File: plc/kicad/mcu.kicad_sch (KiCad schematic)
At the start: 58 parts, among them J1 Conn_01x03_Pin, J2 Conn_01x04_Pin, Q3 L8050QLT1G, Q4 L8050QLT1G, SW1 TSD003B08026A03, SW2 TSD003B08026A03, U10 ESP32-S3-MINI-1U, U11 BS-0601-SK-4W, U12 AHT20_C2757850, U13 CP2102N-A02-GQFN28R, U9 RV-3028-C7

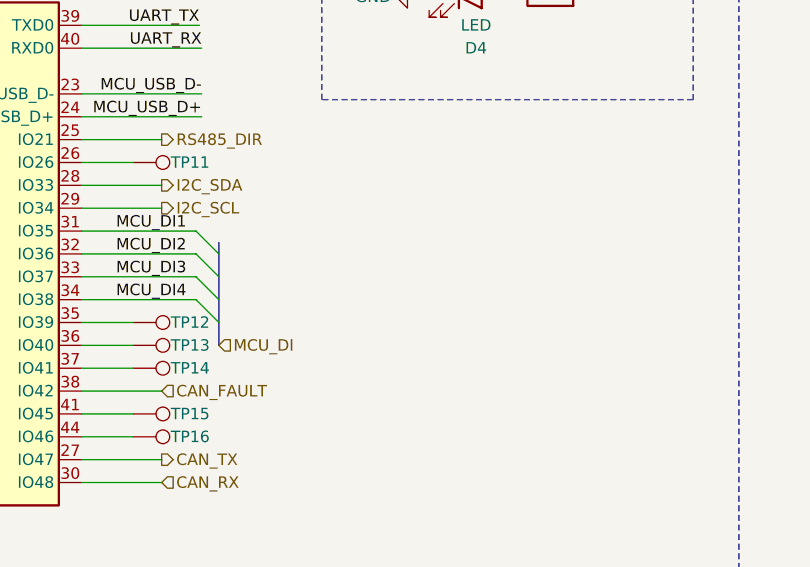
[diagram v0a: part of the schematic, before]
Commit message: Updated PCB placement
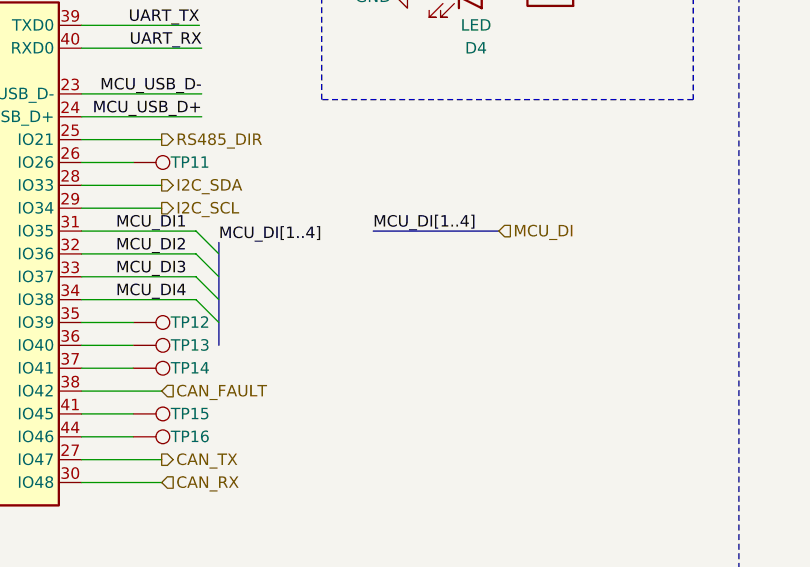
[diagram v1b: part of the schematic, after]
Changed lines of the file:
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@@
+		)
+	)
+	(bus
+		(pts
+			(xy 158.115 72.39) (xy 172.085 72.39)
+		)
+		(stroke
+			(width 0)
+			(type default)
 		)
 	)
@@
 		)
 	)
+	(label "MCU_DI[1..4]"
+		(at 158.115 72.39 0)
+		(effects
+			(font
+				(size 1.27 1.27)
+			)
+			(justify left bottom)
+		)
+	)
 	(label "SD_CD"
 		(at 84.455 77.47 0)
@@
 			)
 			(justify right bottom)
+		)
+	)
+	(label "MCU_DI[1..4]"
+		(at 140.97 73.66 0)
+		(effects
+			(font
+				(size 1.27 1.27)
+			)
+			(justify left bottom)
 		)
 	)
@@
 		)
 	)
+	(hierarchical_label "MCU_DI"
+		(shape input)
+		(at 172.085 72.39 0)
+		(effects
+			(font
+				(size 1.27 1.27)
+			)
+			(justify left)
+		)
+	)
 	(hierarchical_label "I2C_SCL"
 		(shape input)
@@
 		)
 	)
-	(hierarchical_label "MCU_DI"
-		(shape input)
-		(at 140.97 85.09 0)
-		(effects
-			(font
-				(size 1.27 1.27)
-			)
-			(justify left)
-		)
-	)

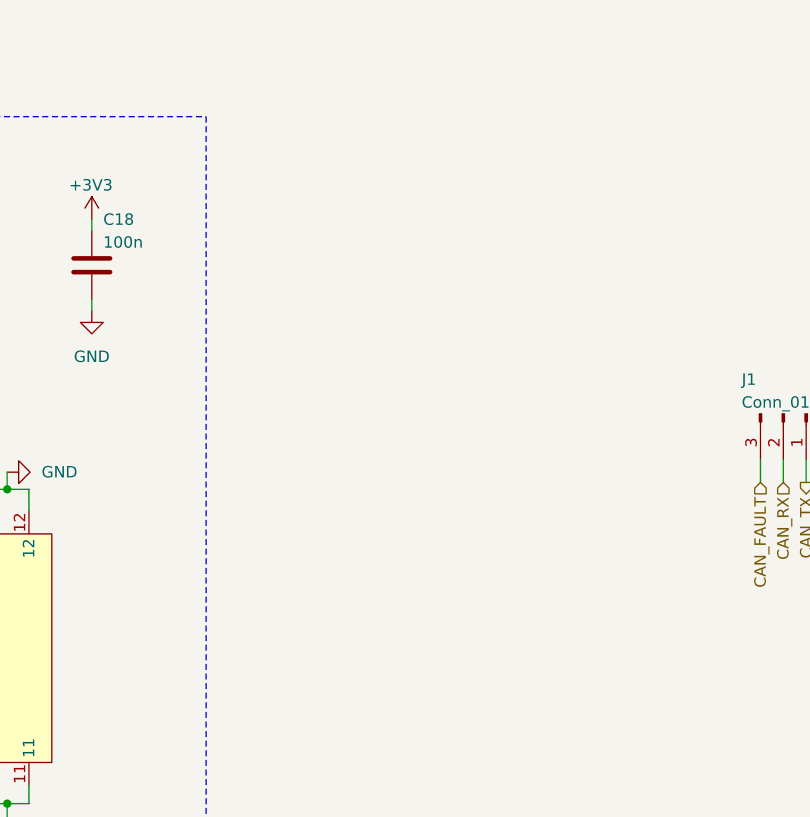
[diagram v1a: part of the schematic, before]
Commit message: Added mounting holes & PCB outline
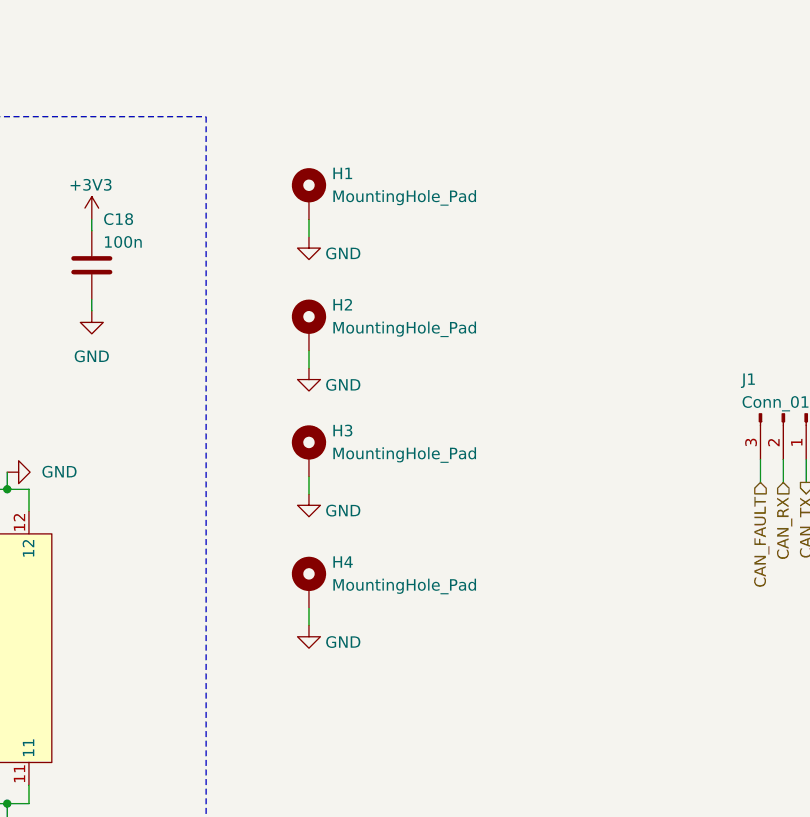
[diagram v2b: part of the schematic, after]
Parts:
- added H1, H2, H3, H4: MountingHole_Pad, MountingHole:MountingHole_4.3mm_M4_DIN965_Pad_TopBottom, symbol Mechanical:MountingHole_Pad
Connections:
- net GND: now also H1.1, H2.1, H3.1, H4.1

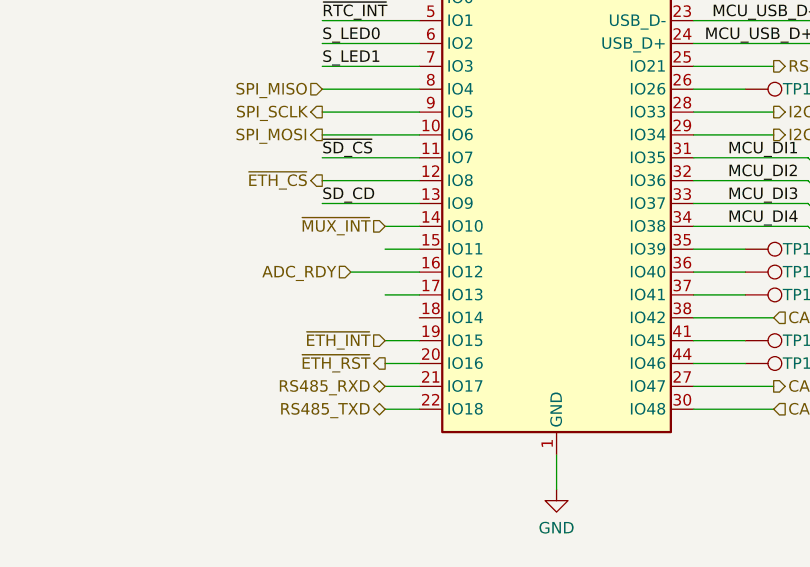
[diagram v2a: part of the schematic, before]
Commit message: Updated PCB placement
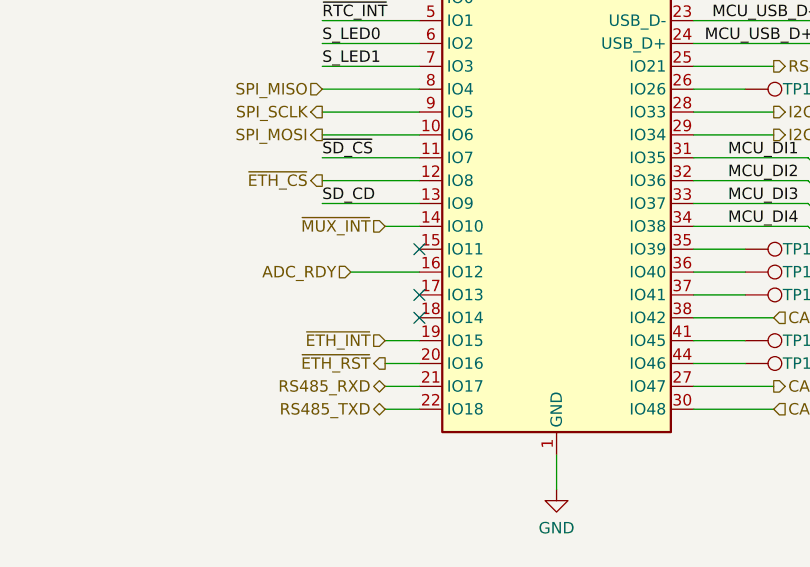
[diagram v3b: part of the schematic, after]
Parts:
- J1: footprint (none) -> Connector_PinHeader_2.54mm:PinHeader_1x03_P2.54mm_Vertical
- J2: footprint Connector_PinSocket_2.54mm:PinSocket_1x04_P2.54mm_Vertical -> Connector_PinHeader_2.54mm:PinHeader_1x04_P2.54mm_Vertical
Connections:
- no-connect marks 25 -> 28
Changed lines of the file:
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@@
 	)
 	(no_connect
+		(at 95.25 82.55)
+	)
+	(no_connect
 		(at 278.384 51.054)
 	)
@@
 		(at 316.484 63.754)
 	)
+	(no_connect
+		(at 95.25 87.63)
+	)
+	(no_connect
+		(at 95.25 90.17)
+	)
 	(bus_entry
 		(at 140.97 82.55)
@@
 	(wire
 		(pts
-			(xy 91.44 87.63) (xy 95.25 87.63)
-		)
-		(stroke
-			(width 0)
-			(type default)
-		)
-	)
-	(wire
-		(pts
 			(xy 91.44 92.71) (xy 95.25 92.71)
 		)
@@
 	(wire
 		(pts
-			(xy 91.44 82.55) (xy 95.25 82.55)
-		)
-		(stroke
-			(width 0)
-			(type default)
-		)
-	)
-	(wire
-		(pts
 			(xy 336.55 106.68) (xy 340.995 106.68)
 		)
@@
 			)
 		)
-		(property "Footprint" "Connector_PinSocket_2.54mm:PinSocket_1x04_P2.54mm_Vertical"
+		(property "Footprint" "Connector_PinHeader_2.54mm:PinHeader_1x04_P2.54mm_Vertical"
 			(at 393.065 225.425 0)
 			(hide yes)
@@
 			)
 		)
-		(property "Footprint" ""
+		(property "Footprint" "Connector_PinHeader_2.54mm:PinHeader_1x03_P2.54mm_Vertical"
 			(at 361.315 225.425 0)
 			(hide yes)

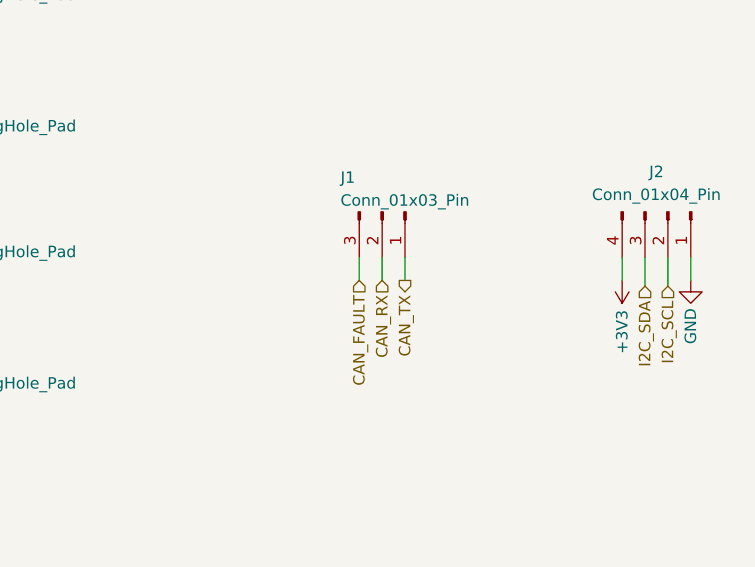
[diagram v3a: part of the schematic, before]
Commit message: Updated switch placement for can & rs485
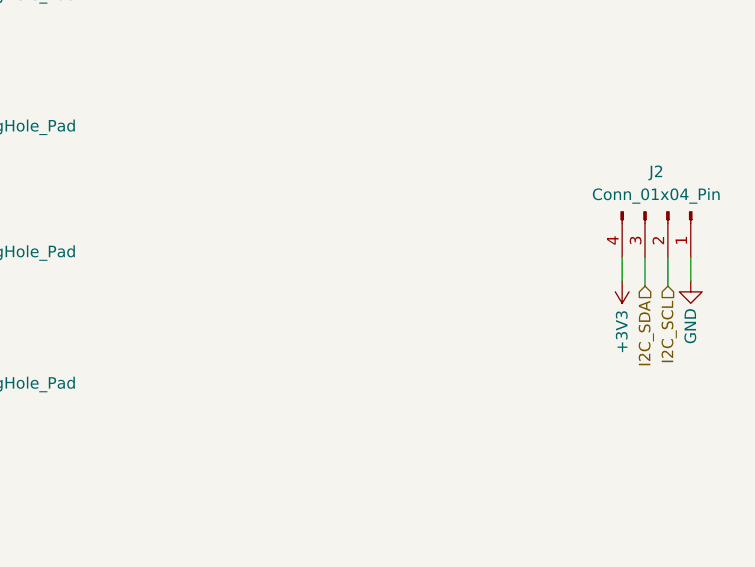
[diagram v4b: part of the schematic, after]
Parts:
- removed J1: Conn_01x03_Pin, Connector_PinHeader_2.54mm:PinHeader_1x03_P2.54mm_Vertical, symbol Connector:Conn_01x03_Pin
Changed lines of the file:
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@@
 	(wire
 		(pts
-			(xy 363.855 233.045) (xy 363.855 230.505)
-		)
-		(stroke
-			(width 0)
-			(type default)
-		)
-	)
-	(wire
-		(pts
 			(xy 84.455 69.85) (xy 95.25 69.85)
 		)
@@
 	(wire
 		(pts
-			(xy 361.315 233.045) (xy 361.315 230.505)
-		)
-		(stroke
-			(width 0)
-			(type default)
-		)
-	)
-	(wire
-		(pts
 			(xy 360.68 72.39) (xy 368.3 72.39)
 		)
@@
 	(wire
 		(pts
-			(xy 358.775 233.045) (xy 358.775 230.505)
-		)
-		(stroke
-			(width 0)
-			(type default)
-		)
-	)
-	(wire
-		(pts
 			(xy 257.81 208.915) (xy 257.81 210.82)
 		)
@@
 		)
 	)
-	(hierarchical_label "CAN_RX"
-		(shape input)
-		(at 361.315 233.045 270)
-		(effects
-			(font
-				(size 1.27 1.27)
-			)
-			(justify right)
-		)
-	)
 	(hierarchical_label "I2C_SCL"
 		(shape output)
@@
 		)
 	)
-	(hierarchical_label "CAN_TX"
-		(shape output)
-		(at 363.855 233.045 270)
-		(effects
-			(font
-				(size 1.27 1.27)
-			)
-			(justify right)
-		)
-	)
 	(hierarchical_label "I2C_SDA"
 		(shape output)
@@
 		)
 	)
-	(hierarchical_label "CAN_FAULT"
-		(shape input)
-		(at 358.775 233.045 270)
-		(effects
-			(font
-				(size 1.27 1.27)
-			)
-			(justify right)
-		)
-	)
 	(hierarchical_label "~{ETH_INT}"
 		(shape input)
@@
 					(unit 1)
 				)
-			)
-		)
-	)
-	(symbol
-		(lib_id "Connector:Conn_01x03_Pin")
-		(at 361.315 225.425 270)
-		(unit 1)
-		(body_style 1)
-		(exclude_from_sim no)
-		(in_bom yes)
-		(on_board yes)
-		(in_pos_files yes)
-		(dnp no)
-		(property "Reference" "J1"
-			(at 357.505 221.615 90)
-			(show_name no)
-			(do_not_autoplace no)
-			(effects
-				(font
-					(size 1.27 1.27)
-				)
-			)
-		)
-		(property "Value" "Conn_01x03_Pin"
-			(at 363.855 224.155 90)
-			(show_name no)
-			(do_not_autoplace no)
-			(effects
-				(font
-					(size 1.27 1.27)
-				)
-			)
-		)
-		(property "Footprint" "Connector_PinHeader_2.54mm:PinHeader_1x03_P2.54mm_Vertical"
-			(at 361.315 225.425 0)
-			(hide yes)
-			(show_name no)
-			(do_not_autoplace no)
-			(effects
-				(font
-					(size 1.27 1.27)
-				)
-			)
-		)
-		(property "Datasheet" ""
-			(at 361.315 225.425 0)
-			(hide yes)
-			(show_name no)
-			(do_not_autoplace no)
-			(effects
-				(font
-					(size 1.27 1.27)
-				)
-			)
-		)
-		(property "Description" "Generic connector, single row, 01x03, script generated"
-			(at 361.315 225.425 0)
-			(hide yes)
-			(show_name no)
-			(do_not_autoplace no)
-			(effects
-				(font
-					(size 1.27 1.27)
-				)
-			)
-		)
-		(pin "3"
-		)
-		(pin "2"
-		)
-		(pin "1"
-		)
-		(instances
-			(project "LibrePLC32"
-				(path "/ef4c1a27-85a3-413a-9f93-a41c4f97eee5/7ef97c26-a6eb-42fc-a9a7-66112d2bed2b"
-					(reference "J1")
-					(unit 1)
-				)

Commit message: Updated PCB placement & graphics
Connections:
- net ~{MCU_BOOT}: now also SW2.1
- net ~{MCU_RST}: now also SW1.1
- no-connect marks 28 -> 26
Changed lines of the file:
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@@
+	)
+	(junction
+		(at 45.085 140.335)
+		(diameter 0)
+		(color 0 0 0 0)
 	)
 	(junction
@@
 	)
 	(junction
+		(at 163.83 140.335)
+		(diameter 0)
+		(color 0 0 0 0)
+	)
+	(junction
 		(at 74.93 191.77)
 		(diameter 0)
@@
 	)
 	(no_connect
-		(at 48.895 152.4)
-	)
-	(no_connect
 		(at 278.384 71.374)
 	)
@@
 	(no_connect
 		(at 316.484 71.374)
-	)
-	(no_connect
-		(at 167.64 152.4)
 	)
 	(no_connect
@@
 	(wire
 		(pts
-			(xy 159.385 140.335) (xy 167.64 140.335)
+			(xy 159.385 140.335) (xy 163.83 140.335)
 		)
 		(stroke
@@
 	(wire
 		(pts
+			(xy 163.83 152.4) (xy 163.83 140.335)
+		)
+		(stroke
+			(width 0)
+			(type default)
+		)
+	)
+	(wire
+		(pts
 			(xy 170.18 270.51) (xy 165.1 270.51)
 		)
@@
 	(wire
 		(pts
+			(xy 45.085 140.335) (xy 48.895 140.335)
+		)
+		(stroke
+			(width 0)
+			(type default)
+		)
+	)
+	(wire
+		(pts
 			(xy 134.62 97.79) (xy 125.73 97.79)
 		)
@@
 	(wire
 		(pts
+			(xy 48.895 152.4) (xy 45.085 152.4)
+		)
+		(stroke
+			(width 0)
+			(type default)
+		)
+	)
+	(wire
+		(pts
 			(xy 297.307 43.434) (xy 297.307 42.164)
 		)
@@
 	(wire
 		(pts
-			(xy 41.275 140.335) (xy 48.895 140.335)
+			(xy 41.275 140.335) (xy 45.085 140.335)
 		)
 		(stroke
@@
 	(wire
 		(pts
+			(xy 45.085 152.4) (xy 45.085 140.335)
+		)
+		(stroke
+			(width 0)
+			(type default)
+		)
+	)
+	(wire
+		(pts
 			(xy 33.02 200.025) (xy 33.02 201.295)
 		)
@@
 	(wire
 		(pts
+			(xy 163.83 140.335) (xy 167.64 140.335)
+		)
+		(stroke
+			(width 0)
+			(type default)
+		)
+	)
+	(wire
+		(pts
 			(xy 350.52 53.975) (xy 353.06 53.975)
 		)
@@
 		)
 		(stroke
+			(width 0)
+			(type default)
+		)
+	)
+	(wire
+		(pts
+			(xy 167.64 152.4) (xy 163.83 152.4)
+		)
+		(stroke
